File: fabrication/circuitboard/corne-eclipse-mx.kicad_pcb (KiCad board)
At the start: 2 copper layers, 275.5 x 105.6 mm, 182 parts, among them J2 OLED, J4 OLED, SW1 SW_MX_HS, SW10 SW_MX_HS, SW11 SW_MX_HS, SW12 SW_MX_HS, SW13 SW_MX_HS, SW14 SW_MX_HS, SW15 SW_MX_HS, SW16 SW_MX_HS, SW17 SW_MX_HS, SW18 SW_MX_HS, SW2 SW_MX_HS, SW20 SW_MX_HS, SW21 SW_MX_HS, SW22 SW_MX_HS, SW23 SW_MX_HS, SW24 SW_MX_HS, SW25 SW_MX_HS, SW26 SW_MX_HS, SW27 SW_MX_HS, SW28 SW_MX_HS, SW29 SW_MX_HS, SW3 SW_MX_HS, SW30 SW_MX_HS, SW31 SW_MX_HS, SW32 SW_MX_HS, SW33 SW_MX_HS, SW34 SW_MX_HS, SW35 SW_MX_HS, SW36 SW_MX_HS, SW37 SW_MX_HS, SW38 SW_MX_HS, SW39 SW_MX_HS, SW4 SW_MX_HS, SW40 SW_MX_HS, SW42 SW_MX_HS, SW43 SW_MX_HS, SW44 SW_MX_HS, SW5 SW_MX_HS, SW6 SW_MX_HS, SW7 SW_MX_HS, SW8 SW_MX_HS, SW9 SW_MX_HS, U1 nice!nano, U2 nice!nano

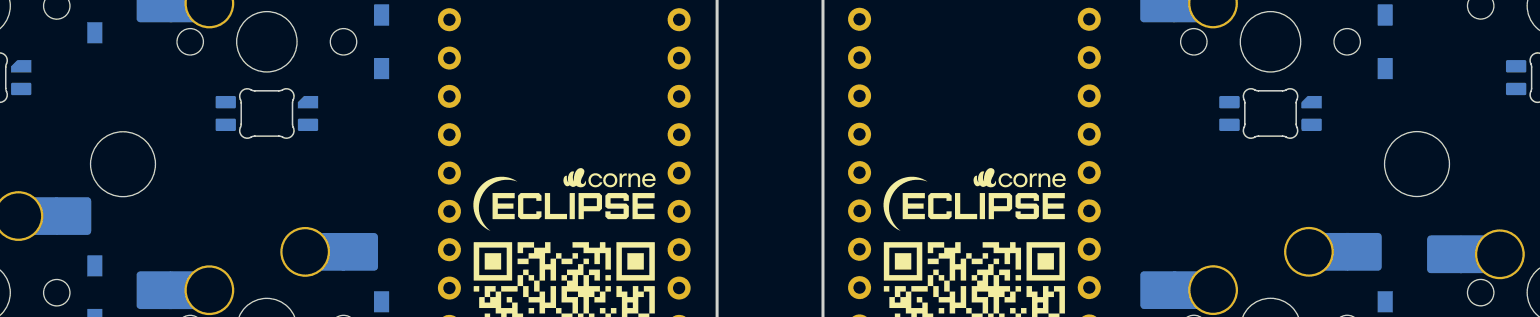
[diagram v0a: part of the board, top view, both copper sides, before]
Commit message: fix(pcb): screw hole alignment to case adjustments
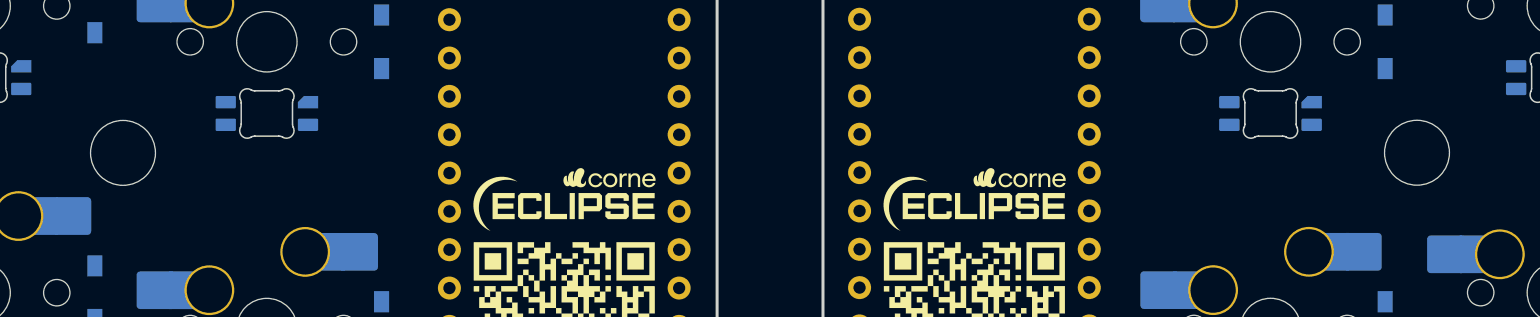
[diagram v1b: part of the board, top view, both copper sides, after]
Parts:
- moved MH1 0.75 mm to (105.6, 40.0)
- moved MH9 0.75 mm to (191.3, 40.0)
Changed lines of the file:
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@@
 	(footprint "kbd:M2_HOLE_v2"
 		(layer "F.Cu")
-		(at 105.5755 40.773711)
+		(at 105.5755 40.023711)
 		(descr "Mounting Hole 2.2mm, no annular, M2")
 		(tags "mounting hole 2.2mm no annular m2")
@@
 	(footprint "kbd:M2_HOLE_v2"
 		(layer "F.Cu")
-		(at 191.3135 40.773711 180)
-		(descr "Mounting Hole 2.2mm, no annular, M2")
-		(tags "mounting hole 2.2mm no annular m2")
+		(at 191.3135 40.023711 180)
+		(descr "Mounting Hole 2.2mm, no annular, M2")
+		(tags "mounting hole 2.2mm no annular m2")

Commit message: fix(pcbs): aligned screw holes on lp and mx
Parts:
- moved MH11 0.20 mm to (29.6, 44.5)
- moved MH8 0.20 mm to (267.3, 44.5)
- moved MH10 0.20 mm to (27.5, 53.3)
- moved MH13 0.20 mm to (269.4, 53.3)
- moved MH1 0.15 mm to (105.6, 40.2)
- moved MH9 0.15 mm to (191.3, 40.2)
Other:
- outline, holes or cut-outs redrawn
